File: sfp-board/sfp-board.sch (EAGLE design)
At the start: 20 parts

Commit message: board with logo & update .gitgnore for ingoring tempoary file
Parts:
- added U$1: BRS-SYMBOL, digital-toy:BRS-SYMBOL
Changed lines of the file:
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@@
 <part name="P+8" library="supply1" deviceset="VCC" device=""/>
 <part name="GND10" library="supply1" deviceset="GND" device=""/>
+<part name="U$1" library="digital-toy" deviceset="BRS-SYMBOL" device=""/>
 </parts>
 <sheets>
@@
 <attribute name="VALUE" x="48.26" y="86.36" size="1.778" layer="96" rot="R90"/>
 </instance>
+<instance part="U$1" gate="G$1" x="30.48" y="55.88"/>
 </instances>
 <busses>

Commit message: Board v13
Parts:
- removed C1: capacitor, digital-toy:CAPPTH3
- removed R3: 150ohm, rcl:R-US_0411/15
- added JP1: (no value), SparkFun:M02PTH3
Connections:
- net GND: now also JP1.2; no longer C1.2
- net N$4: now also GP2Y1010AU0F.VCC, WEMOS1.3V3; no longer C1.1, R3.2
- net VCC: now also JP1.1; no longer GP2Y1010AU0F.VCC, R3.1
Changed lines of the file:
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@@
 <part name="P+2" library="supply1" deviceset="VCC" device=""/>
 <part name="GND6" library="supply1" deviceset="GND" device=""/>
-<part name="P+3" library="supply1" deviceset="VCC" device=""/>
 <part name="P+4" library="supply1" deviceset="VCC" device=""/>
 <part name="P+5" library="supply1" deviceset="VCC" device=""/>
-<part name="R3" library="rcl" deviceset="R-US_" device="0411/15" value="150ohm"/>
-<part name="P+6" library="supply1" deviceset="VCC" device=""/>
-<part name="C1" library="digital-toy" deviceset="CAP" device="PTH3" value="capacitor"/>
 <part name="H1" library="holes" deviceset="MOUNT-HOLE" device="3.3"/>
 <part name="H2" library="holes" deviceset="MOUNT-HOLE" device="3.3"/>
@@
 <part name="GND10" library="supply1" deviceset="GND" device=""/>
 <part name="U$1" library="digital-toy" deviceset="BRS-SYMBOL" device=""/>
+<part name="JP1" library="SparkFun" deviceset="M02" device="PTH3"/>
+<part name="P+9" library="supply1" deviceset="VCC" device=""/>
+<part name="GND11" library="supply1" deviceset="GND" device=""/>
 </parts>
 <sheets>
@@
 <attribute name="VALUE" x="-10.16" y="25.4" size="1.778" layer="96" rot="R90"/>
 </instance>
-<instance part="P+3" gate="VCC" x="-10.16" y="17.78" smashed="yes" rot="R270">
-<attribute name="VALUE" x="-12.7" y="20.32" size="1.778" layer="96"/>
-</instance>
 <instance part="P+4" gate="VCC" x="35.56" y="25.4" smashed="yes" rot="R270">
 <attribute name="VALUE" x="30.48" y="22.86" size="1.778" layer="96"/>
@@
 <instance part="P+5" gate="VCC" x="45.72" y="33.02" smashed="yes" rot="R90">
 <attribute name="VALUE" x="48.26" y="30.48" size="1.778" layer="96" rot="R180"/>
-</instance>
-<instance part="R3" gate="G$1" x="-20.32" y="50.8" smashed="yes" rot="R270">
-<attribute name="NAME" x="-18.8214" y="52.07" size="1.778" layer="95" rot="R270"/>
-<attribute name="VALUE" x="-23.622" y="54.61" size="1.778" layer="96" rot="R270"/>
-</instance>
-<instance part="P+6" gate="VCC" x="-20.32" y="58.42" smashed="yes">
-<attribute name="VALUE" x="-22.86" y="55.88" size="1.778" layer="96" rot="R90"/>
-</instance>
-<instance part="C1" gate="G$1" x="-15.24" y="40.64" smashed="yes">
-<attribute name="NAME" x="-17.653" y="39.116" size="1.27" layer="95" rot="R90"/>
-<attribute name="VALUE" x="-11.811" y="41.402" size="1.27" layer="96" rot="R90"/>
 </instance>
 <instance part="H1" gate="G$1" x="55.88" y="106.68"/>
@@
 </instance>
 <instance part="U$1" gate="G$1" x="30.48" y="55.88"/>
+<instance part="JP1" gate="G$1" x="76.2" y="66.04" rot="R180"/>
+<instance part="P+9" gate="VCC" x="66.04" y="68.58" smashed="yes" rot="R90">
+<attribute name="VALUE" x="66.04" y="68.58" size="1.778" layer="96" rot="R180"/>
+</instance>
+<instance part="GND11" gate="1" x="66.04" y="60.96" smashed="yes" rot="R270">
+<attribute name="VALUE" x="60.96" y="60.96" size="1.778" layer="96"/>
+</instance>
 </instances>
 <busses>
@@
 <pinref part="GND4" gate="1" pin="GND"/>
 <wire x1="-15.24" y1="38.1" x2="-22.86" y2="38.1" width="0.1524" layer="91"/>
-<pinref part="C1" gate="G$1" pin="2"/>
-<wire x1="-15.24" y1="40.64" x2="-15.24" y2="38.1" width="0.1524" layer="91"/>
-<junction x="-15.24" y="38.1"/>
 </segment>
 <segment>
@@
 <wire x1="43.18" y1="88.9" x2="40.64" y2="88.9" width="0.1524" layer="91"/>
 </segment>
+<segment>
+<pinref part="JP1" gate="G$1" pin="2"/>
+<pinref part="GND11" gate="1" pin="GND"/>
+<wire x1="68.58" y1="60.96" x2="68.58" y2="63.5" width="0.1524" layer="91"/>
+</segment>
 </net>
 <net name="VCC" class="0">
@@
 </segment>
 <segment>
-<pinref part="GP2Y1010AU0F" gate="G$1" pin="VCC"/>
-<pinref part="P+3" gate="VCC" pin="VCC"/>
-<wire x1="-12.7" y1="17.78" x2="-22.86" y2="17.78" width="0.1524" layer="91"/>
-</segment>
-<segment>
 <pinref part="WEMOS1" gate="D1" pin="5V"/>
 <pinref part="P+4" gate="VCC" pin="VCC"/>
@@
 </segment>
 <segment>
-<pinref part="R3" gate="G$1" pin="1"/>
-<pinref part="P+6" gate="VCC" pin="VCC"/>
-</segment>
-<segment>
 <pinref part="R2" gate="G$1" pin="2"/>
 <pinref part="P+7" gate="VCC" pin="VCC"/>
@@
 <pinref part="P+8" gate="VCC" pin="VCC"/>
 </segment>
-</net>
-<net name="N$1" class="0">
-<segment>
-<pinref part="GP2Y1010AU0F" gate="G$1" pin="VOUT"/>
-<wire x1="-22.86" y1="22.86" x2="-7.62" y2="22.86" width="0.1524" layer="91"/>
-<wire x1="-7.62" y1="22.86" x2="-7.62" y2="40.64" width="0.1524" layer="91"/>
-<pinref part="WEMOS1" gate="D1" pin="A0"/>
-<wire x1="-7.62" y1="40.64" x2="-2.54" y2="40.64" width="0.1524" layer="91"/>
+<segment>
+<pinref part="JP1" gate="G$1" pin="1"/>
+<pinref part="P+9" gate="VCC" pin="VCC"/>
+<wire x1="68.58" y1="68.58" x2="68.58" y2="66.04" width="0.1524" layer="91"/>
 </segment>
 </net>
@@
 <segment>
 <pinref part="GP2Y1010AU0F" gate="G$1" pin="V-LED"/>
-<wire x1="-22.86" y1="43.18" x2="-20.32" y2="43.18" width="0.1524" layer="91"/>
-<pinref part="R3" gate="G$1" pin="2"/>
-<wire x1="-20.32" y1="43.18" x2="-20.32" y2="45.72" width="0.1524" layer="91"/>
-<pinref part="C1" gate="G$1" pin="1"/>
-<wire x1="-15.24" y1="43.18" x2="-15.24" y2="45.72" width="0.1524" layer="91"/>
-<wire x1="-15.24" y1="45.72" x2="-20.32" y2="45.72" width="0.1524" layer="91"/>
-<junction x="-20.32" y="45.72"/>
+<wire x1="-22.86" y1="43.18" x2="-6.604" y2="43.18" width="0.1524" layer="91"/>
+<wire x1="-6.604" y1="43.18" x2="-6.604" y2="25.4" width="0.1524" layer="91"/>
+<pinref part="GP2Y1010AU0F" gate="G$1" pin="VCC"/>
+<wire x1="-22.86" y1="17.78" x2="-2.54" y2="17.78" width="0.1524" layer="91"/>
+<pinref part="WEMOS1" gate="D1" pin="3V3"/>
+<wire x1="-2.54" y1="17.78" x2="-2.54" y2="25.4" width="0.1524" layer="91"/>
+<wire x1="-6.604" y1="25.4" x2="-2.54" y2="25.4" width="0.1524" layer="91"/>
+<junction x="-2.54" y="25.4"/>
 </segment>
 </net>
@@
 </segment>
 </net>
+<net name="N$14" class="0">
+<segment>
+<pinref part="WEMOS1" gate="D1" pin="A0"/>
+<wire x1="-2.54" y1="40.64" x2="-5.08" y2="40.64" width="0.1524" layer="91"/>
+<pinref part="GP2Y1010AU0F" gate="G$1" pin="VOUT"/>
+<wire x1="-5.08" y1="40.64" x2="-5.842" y2="40.64" width="0.1524" layer="91"/>
+<wire x1="-22.86" y1="22.86" x2="-7.62" y2="22.86" width="0.1524" layer="91"/>
+<wire x1="-5.842" y1="40.64" x2="-7.62" y2="40.64" width="0.1524" layer="91"/>
+<wire x1="-7.62" y1="40.64" x2="-7.62" y2="22.86" width="0.1524" layer="91"/>
+</segment>
+</net>

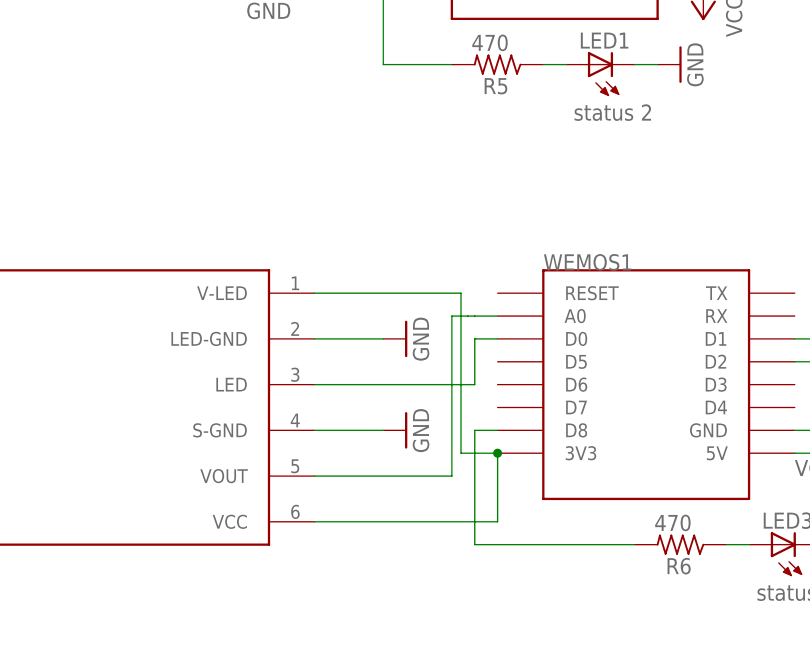
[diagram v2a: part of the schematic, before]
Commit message: board v14 with new dustsensor reader
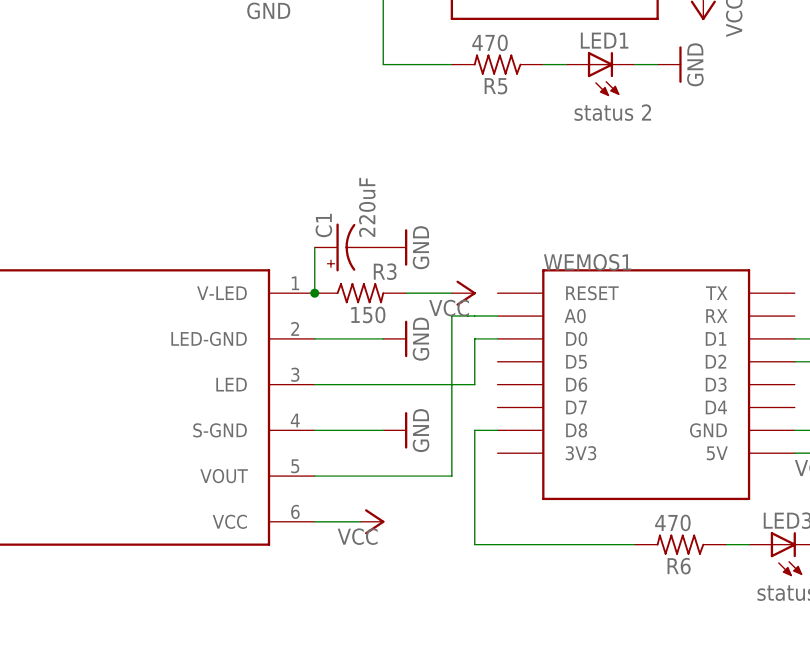
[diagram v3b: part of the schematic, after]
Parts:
- added C1: 220uF, SparkFun:CAP_POLPTH1
- added R3: 150, rcl:R-US_0411/15
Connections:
- new net N$1: C1.+, GP2Y1010AU0F.V-LED, R3.1
- net GND: now also C1.-
- net N$14: no longer WEMOS1.A0
- net N$4: now also WEMOS1.A0; no longer GP2Y1010AU0F.V-LED, GP2Y1010AU0F.VCC, WEMOS1.3V3
- net VCC: now also GP2Y1010AU0F.VCC, R3.2
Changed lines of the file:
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@@
 <part name="P+9" library="supply1" deviceset="VCC" device=""/>
 <part name="GND11" library="supply1" deviceset="GND" device=""/>
+<part name="C1" library="SparkFun" deviceset="CAP_POL" device="PTH1" value="220uF"/>
+<part name="R3" library="rcl" deviceset="R-US_" device="0411/15" value="150"/>
+<part name="GND12" library="supply1" deviceset="GND" device=""/>
+<part name="P+3" library="supply1" deviceset="VCC" device=""/>
+<part name="P+6" library="supply1" deviceset="VCC" device=""/>
 </parts>
 <sheets>
@@
 <attribute name="VALUE" x="53.34" y="50.8" size="1.778" layer="96" rot="R180"/>
 </instance>
-<instance part="GND4" gate="1" x="-12.7" y="38.1" smashed="yes" rot="R90">
-<attribute name="VALUE" x="-10.16" y="35.56" size="1.778" layer="96" rot="R90"/>
+<instance part="GND4" gate="1" x="-12.7" y="48.26" smashed="yes" rot="R90">
+<attribute name="VALUE" x="-10.16" y="45.72" size="1.778" layer="96" rot="R90"/>
 </instance>
 <instance part="GND5" gate="1" x="25.4" y="81.28" smashed="yes" rot="R90">
@@
 <attribute name="VALUE" x="60.96" y="60.96" size="1.778" layer="96"/>
 </instance>
+<instance part="C1" gate="G$1" x="-20.32" y="48.26" smashed="yes" rot="R90">
+<attribute name="NAME" x="-20.955" y="49.276" size="1.778" layer="95" rot="R90"/>
+<attribute name="VALUE" x="-16.129" y="49.276" size="1.778" layer="96" rot="R90"/>
+</instance>
+<instance part="R3" gate="G$1" x="-17.78" y="43.18" smashed="yes">
+<attribute name="NAME" x="-16.51" y="44.6786" size="1.778" layer="95"/>
+<attribute name="VALUE" x="-19.05" y="39.878" size="1.778" layer="96"/>
+</instance>
+<instance part="GND12" gate="1" x="-12.7" y="38.1" smashed="yes" rot="R90">
+<attribute name="VALUE" x="-10.16" y="35.56" size="1.778" layer="96" rot="R90"/>
+</instance>
+<instance part="P+3" gate="VCC" x="-15.24" y="17.78" smashed="yes" rot="R270">
+<attribute name="VALUE" x="-20.32" y="15.24" size="1.778" layer="96"/>
+</instance>
+<instance part="P+6" gate="VCC" x="-5.08" y="43.18" smashed="yes" rot="R270">
+<attribute name="VALUE" x="-10.16" y="40.64" size="1.778" layer="96"/>
+</instance>
 </instances>
 <busses>
@@
 </segment>
 <segment>
-<pinref part="GP2Y1010AU0F" gate="G$1" pin="LED-GND"/>
 <pinref part="GND4" gate="1" pin="GND"/>
-<wire x1="-15.24" y1="38.1" x2="-22.86" y2="38.1" width="0.1524" layer="91"/>
+<pinref part="C1" gate="G$1" pin="-"/>
 </segment>
 <segment>
@@
 <wire x1="68.58" y1="60.96" x2="68.58" y2="63.5" width="0.1524" layer="91"/>
 </segment>
+<segment>
+<pinref part="GP2Y1010AU0F" gate="G$1" pin="LED-GND"/>
+<pinref part="GND12" gate="1" pin="GND"/>
+<wire x1="-15.24" y1="38.1" x2="-22.86" y2="38.1" width="0.1524" layer="91"/>
+</segment>
 </net>
 <net name="VCC" class="0">
@@
 <pinref part="P+9" gate="VCC" pin="VCC"/>
 <wire x1="68.58" y1="68.58" x2="68.58" y2="66.04" width="0.1524" layer="91"/>
+</segment>
+<segment>
+<pinref part="GP2Y1010AU0F" gate="G$1" pin="VCC"/>
+<pinref part="P+3" gate="VCC" pin="VCC"/>
+<wire x1="-17.78" y1="17.78" x2="-22.86" y2="17.78" width="0.1524" layer="91"/>
+</segment>
+<segment>
+<pinref part="R3" gate="G$1" pin="2"/>
+<pinref part="P+6" gate="VCC" pin="VCC"/>
+<wire x1="-7.62" y1="43.18" x2="-12.7" y2="43.18" width="0.1524" layer="91"/>
 </segment>
 </net>
@@
 <pinref part="WEMOS1" gate="D1" pin="D0"/>
 <wire x1="-5.08" y1="38.1" x2="-2.54" y2="38.1" width="0.1524" layer="91"/>
-</segment>
-</net>
-<net name="N$4" class="0">
-<segment>
-<pinref part="GP2Y1010AU0F" gate="G$1" pin="V-LED"/>
-<wire x1="-22.86" y1="43.18" x2="-6.604" y2="43.18" width="0.1524" layer="91"/>
-<wire x1="-6.604" y1="43.18" x2="-6.604" y2="25.4" width="0.1524" layer="91"/>
-<pinref part="GP2Y1010AU0F" gate="G$1" pin="VCC"/>
-<wire x1="-22.86" y1="17.78" x2="-2.54" y2="17.78" width="0.1524" layer="91"/>
-<pinref part="WEMOS1" gate="D1" pin="3V3"/>
-<wire x1="-2.54" y1="17.78" x2="-2.54" y2="25.4" width="0.1524" layer="91"/>
-<wire x1="-6.604" y1="25.4" x2="-2.54" y2="25.4" width="0.1524" layer="91"/>
-<junction x="-2.54" y="25.4"/>
 </segment>
 </net>
@@
 <net name="N$14" class="0">
 <segment>
+<pinref part="GP2Y1010AU0F" gate="G$1" pin="VOUT"/>
+<wire x1="-22.86" y1="22.86" x2="-7.62" y2="22.86" width="0.1524" layer="91"/>
+<wire x1="-7.62" y1="40.64" x2="-7.62" y2="22.86" width="0.1524" layer="91"/>
+</segment>
+</net>
+<net name="N$1" class="0">
+<segment>
+<pinref part="C1" gate="G$1" pin="+"/>
+<pinref part="GP2Y1010AU0F" gate="G$1" pin="V-LED"/>
+<wire x1="-22.86" y1="43.18" x2="-22.86" y2="48.26" width="0.1524" layer="91"/>
+<pinref part="R3" gate="G$1" pin="1"/>
+<junction x="-22.86" y="43.18"/>
+</segment>
+</net>
+<net name="N$4" class="0">
+<segment>
 <pinref part="WEMOS1" gate="D1" pin="A0"/>
 <wire x1="-2.54" y1="40.64" x2="-5.08" y2="40.64" width="0.1524" layer="91"/>
-<pinref part="GP2Y1010AU0F" gate="G$1" pin="VOUT"/>
 <wire x1="-5.08" y1="40.64" x2="-5.842" y2="40.64" width="0.1524" layer="91"/>
-<wire x1="-22.86" y1="22.86" x2="-7.62" y2="22.86" width="0.1524" layer="91"/>
 <wire x1="-5.842" y1="40.64" x2="-7.62" y2="40.64" width="0.1524" layer="91"/>
-<wire x1="-7.62" y1="40.64" x2="-7.62" y2="22.86" width="0.1524" layer="91"/>
-</segment>
-</net>
+</segment>
+</net>

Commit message: Board v16 with 4th Gen Code
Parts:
- JP1: value (none) -> POWER
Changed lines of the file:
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@@
 <part name="GND10" library="supply1" deviceset="GND" device=""/>
 <part name="U$1" library="digital-toy" deviceset="BRS-SYMBOL" device=""/>
-<part name="JP1" library="SparkFun" deviceset="M02" device="PTH3"/>
+<part name="JP1" library="SparkFun" deviceset="M02" device="PTH3" value="POWER"/>
 <part name="P+9" library="supply1" deviceset="VCC" device=""/>
 <part name="GND11" library="supply1" deviceset="GND" device=""/>

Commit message: Board v17
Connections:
- removed net N$14: GP2Y1010AU0F.VOUT
- net N$4: now also GP2Y1010AU0F.VOUT
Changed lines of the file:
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@@
 <attribute name="VALUE" x="53.34" y="50.8" size="1.778" layer="96" rot="R180"/>
 </instance>
-<instance part="GND4" gate="1" x="-12.7" y="48.26" smashed="yes" rot="R90">
-<attribute name="VALUE" x="-10.16" y="45.72" size="1.778" layer="96" rot="R90"/>
+<instance part="GND4" gate="1" x="-10.16" y="50.8" smashed="yes" rot="R90">
+<attribute name="VALUE" x="-7.62" y="48.26" size="1.778" layer="96" rot="R90"/>
 </instance>
 <instance part="GND5" gate="1" x="25.4" y="81.28" smashed="yes" rot="R90">
@@
 <attribute name="VALUE" x="-20.32" y="15.24" size="1.778" layer="96"/>
 </instance>
-<instance part="P+6" gate="VCC" x="-5.08" y="43.18" smashed="yes" rot="R270">
-<attribute name="VALUE" x="-10.16" y="40.64" size="1.778" layer="96"/>
+<instance part="P+6" gate="VCC" x="-7.62" y="43.18" smashed="yes" rot="R270">
+<attribute name="VALUE" x="-10.16" y="45.72" size="1.778" layer="96"/>
 </instance>
 </instances>
@@
 <pinref part="GND4" gate="1" pin="GND"/>
 <pinref part="C1" gate="G$1" pin="-"/>
+<wire x1="-12.7" y1="50.8" x2="-15.24" y2="48.26" width="0.1524" layer="91"/>
 </segment>
 <segment>
@@
 <pinref part="R3" gate="G$1" pin="2"/>
 <pinref part="P+6" gate="VCC" pin="VCC"/>
-<wire x1="-7.62" y1="43.18" x2="-12.7" y2="43.18" width="0.1524" layer="91"/>
+<wire x1="-10.16" y1="43.18" x2="-12.7" y2="43.18" width="0.1524" layer="91"/>
 </segment>
 </net>
@@
 </segment>
 </net>
-<net name="N$14" class="0">
-<segment>
-<pinref part="GP2Y1010AU0F" gate="G$1" pin="VOUT"/>
-<wire x1="-22.86" y1="22.86" x2="-7.62" y2="22.86" width="0.1524" layer="91"/>
-<wire x1="-7.62" y1="40.64" x2="-7.62" y2="22.86" width="0.1524" layer="91"/>
-</segment>
-</net>
 <net name="N$1" class="0">
 <segment>
@@
 <net name="N$4" class="0">
 <segment>
+<pinref part="GP2Y1010AU0F" gate="G$1" pin="VOUT"/>
+<wire x1="-22.86" y1="22.86" x2="-7.62" y2="22.86" width="0.1524" layer="91"/>
+<wire x1="-7.62" y1="22.86" x2="-7.62" y2="38.1" width="0.1524" layer="91"/>
 <pinref part="WEMOS1" gate="D1" pin="A0"/>
-<wire x1="-2.54" y1="40.64" x2="-5.08" y2="40.64" width="0.1524" layer="91"/>
-<wire x1="-5.08" y1="40.64" x2="-5.842" y2="40.64" width="0.1524" layer="91"/>
-<wire x1="-5.842" y1="40.64" x2="-7.62" y2="40.64" width="0.1524" layer="91"/>
-</segment>
-</net>
+<wire x1="-7.62" y1="38.1" x2="-2.54" y2="40.64" width="0.1524" layer="91"/>
+</segment>
+</net>
